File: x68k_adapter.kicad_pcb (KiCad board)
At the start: 2 copper layers, 29 parts, among them J1 USB_A, J2 USB_A, J3 SWD, J4 UART, J5 X68k conn, SW1 SW_Push, U1 PGA2040, U2 USB2422, U3 TPD2EUSB30, U4 TPD2EUSB30, Y1 24MHz

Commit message: recover autosave
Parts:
- C1, C11, C5: footprint Capacitor_THT:C_Disc_D7.5mm_W2.5mm_P5.00mm -> Capacitor_THT:C_Disc_D4.3mm_W1.9mm_P5.00mm
- C10, C12: footprint Capacitor_THT:CP_Radial_D8.0mm_P5.00mm -> Capacitor_THT:CP_Radial_D4.0mm_P2.00mm
- R2, R3, R4: footprint Resistor_THT:R_Axial_DIN0204_L3.6mm_D1.6mm_P7.62mm_Horizontal -> Resistor_SMD:R_0603_1608Metric_Pad0.98x0.95mm_HandSolder; moved to B.Cu
- moved C12 155.5 mm to (191.1, 48.3)
- moved C10 146.6 mm to (198.7, 111.8)
- moved C6 64.5 mm to (103.7, 85.3), turned to 180 degrees
- moved C1 51.7 mm to (111.0, 60.2), turned to 180 degrees
- moved R4 43.0 mm to (94.3, 65.4), turned to 180 degrees
- moved R3 42.4 mm to (94.3, 63.4), turned to 180 degrees
- moved F2 35.9 mm to (183.9, 111.8)
- moved R2 34.9 mm to (99.0, 66.9), turned to 180 degrees
- moved C9 31.4 mm to (186.4, 104.1)
- moved C8 28.9 mm to (87.9, 106.7)
- moved F1 27.4 mm to (181.4, 43.2)
- moved Y1 26.0 mm to (110.0, 79.2), turned to 180 degrees
- moved U4 25.4 mm to (172.4, 106.3)
- moved U3 25.0 mm to (168.1, 40.6), turned to 90 degrees
- moved C5 18.6 mm to (121.2, 73.8), turned to 180 degrees
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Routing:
- net Net-(U2-XTALOUT/CLKIN_EN): track 0.00 -> 18.7 mm
- net Net-(U2-XTALIN/CLKIN): track 0.00 -> 18.6 mm
- net Net-(U2-PLLFILT): track 0.00 -> 12.8 mm
- net Net-(U2-SMBDATA/NON_REM1): track 0.00 -> 11.0 mm, vias 0 -> 1
- net Net-(U2-SMBCLK/CFG_SEL0): track 0.00 -> 10.4 mm, vias 0 -> 1
- net Net-(U2-RBIAS): track 0.00 -> 9.37 mm
- net Net-(U2-SUSP/NON_REM0): track 0.00 -> 5.67 mm, vias 0 -> 1

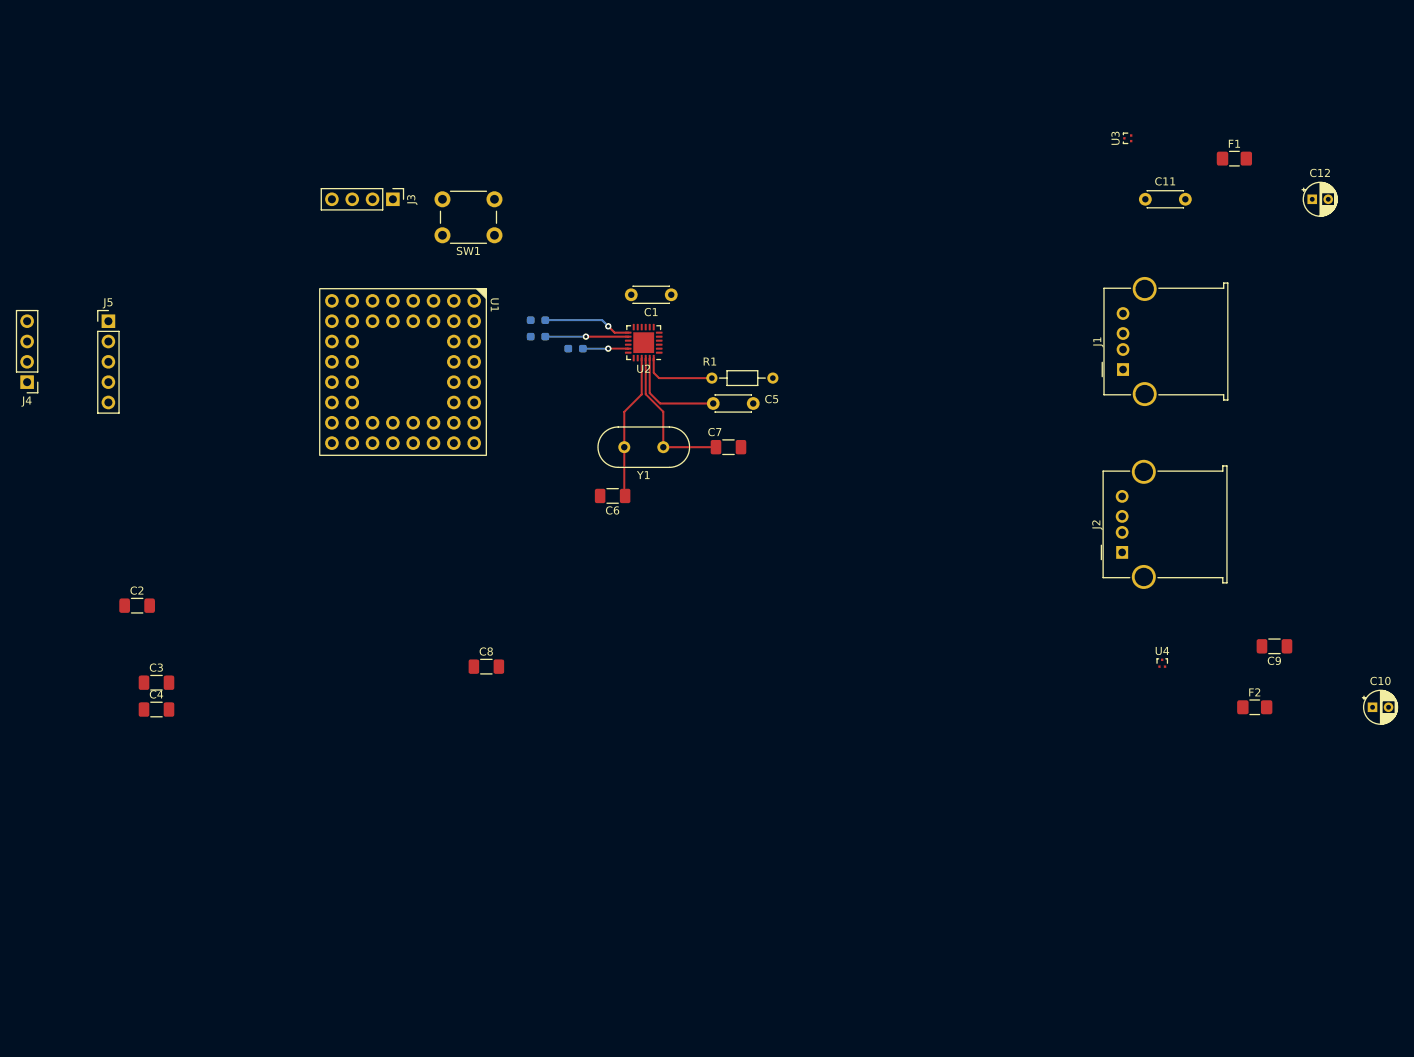
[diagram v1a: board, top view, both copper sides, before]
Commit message: General placement of the components
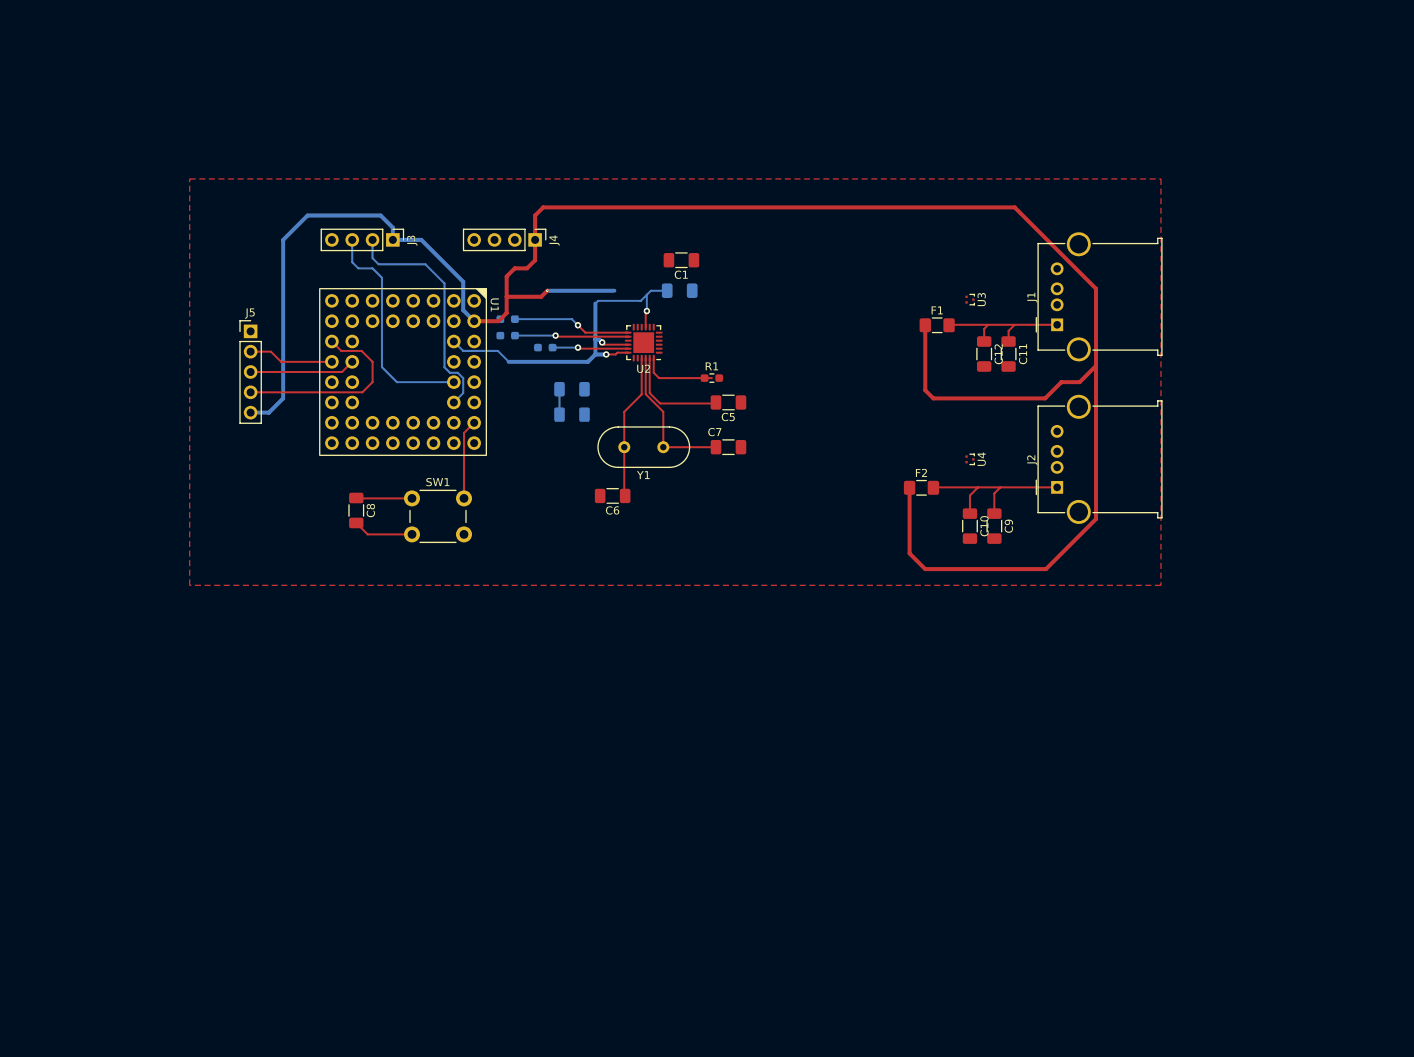
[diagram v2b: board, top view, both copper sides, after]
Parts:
- C1, C11, C5: footprint Capacitor_THT:C_Disc_D4.3mm_W1.9mm_P5.00mm -> Capacitor_SMD:C_1206_3216Metric_Pad1.33x1.80mm_HandSolder
- C10, C12: footprint Capacitor_THT:CP_Radial_D4.0mm_P2.00mm -> Capacitor_SMD:C_1206_3216Metric_Pad1.33x1.80mm_HandSolder
- C2, C3, C4: moved to B.Cu
- R1: footprint Resistor_THT:R_Axial_DIN0204_L3.6mm_D1.6mm_P7.62mm_Horizontal -> Resistor_SMD:R_0603_1608Metric_Pad0.98x0.95mm_HandSolder
- moved C4 83.8 mm to (112.1, 59.7)
- moved J4 65.9 mm to (94.0, 53.3), turned to -90 degrees
- moved C3 61.8 mm to (98.6, 75.2)
- moved C2 60.7 mm to (98.6, 72.0)
- moved C10 55.2 mm to (148.3, 89.1), turned to -90 degrees
- moved F2 49.9 mm to (142.3, 84.3)
- moved C12 45.3 mm to (150.1, 67.6), turned to -90 degrees
- moved F1 42.6 mm to (144.2, 64.0)
- moved C9 38.1 mm to (151.4, 89.1), turned to -90 degrees
- moved U4 35.0 mm to (148.3, 80.8), turned to -90 degrees
- moved SW1 34.5 mm to (78.6, 85.7), turned to 0 degrees
- moved U3 28.2 mm to (148.3, 60.8), turned to -90 degrees
- moved C11 25.8 mm to (153.2, 67.6), turned to -90 degrees
- moved C8 25.4 mm to (71.6, 87.2), turned to -90 degrees
- moved J5 17.8 mm to (58.4, 64.8)
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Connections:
- J4 pad 2: /Tx -> /U_Tx
- J4 pad 3: /Rx -> /U_Rx
- U1 pad B1: /Tx -> /U_Tx
- U1 pad C1: /Rx -> /U_Rx
- U2 pad 2: Net-(J1-D-) -> Net-(J2-D-)
- U2 pad 3: Net-(J1-D+) -> Net-(J2-D+)
- U2 pad 4: Net-(J2-D-) -> Net-(J1-D-)
- U2 pad 5: Net-(J2-D+) -> Net-(J1-D+)
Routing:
- net +5V: track 0.00 -> 261.0 mm, vias 0 -> 1
- net +3V3: track 0.00 -> 51.0 mm, vias 0 -> 3
- net Net-(J3-Pin_2): track 0.00 -> 29.5 mm
- net Net-(J3-Pin_3): track 0.00 -> 28.2 mm
- net /Tx: track 0.00 -> 24.4 mm
- net Net-(J2-VBUS): track 0.00 -> 22.8 mm
- net Net-(J1-VBUS): track 0.00 -> 18.2 mm
- net Net-(U1-BOOTSEL): track 0.00 -> 17.0 mm
- net /Rx: track 0.00 -> 13.2 mm
- net /Mouse: track 0.00 -> 10.7 mm
- net GND: track 0.00 -> 7.55 mm
- net Net-(U2-SUSP/NON_REM0): track 5.67 -> 9.51 mm
- net Net-(U2-SMBCLK/CFG_SEL0): track 10.4 -> 14.2 mm
- net Net-(U2-SMBDATA/NON_REM1): track 11.0 -> 14.9 mm
- added copper zone on F.Cu, net GND

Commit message: Add LCD and finish USB DPs
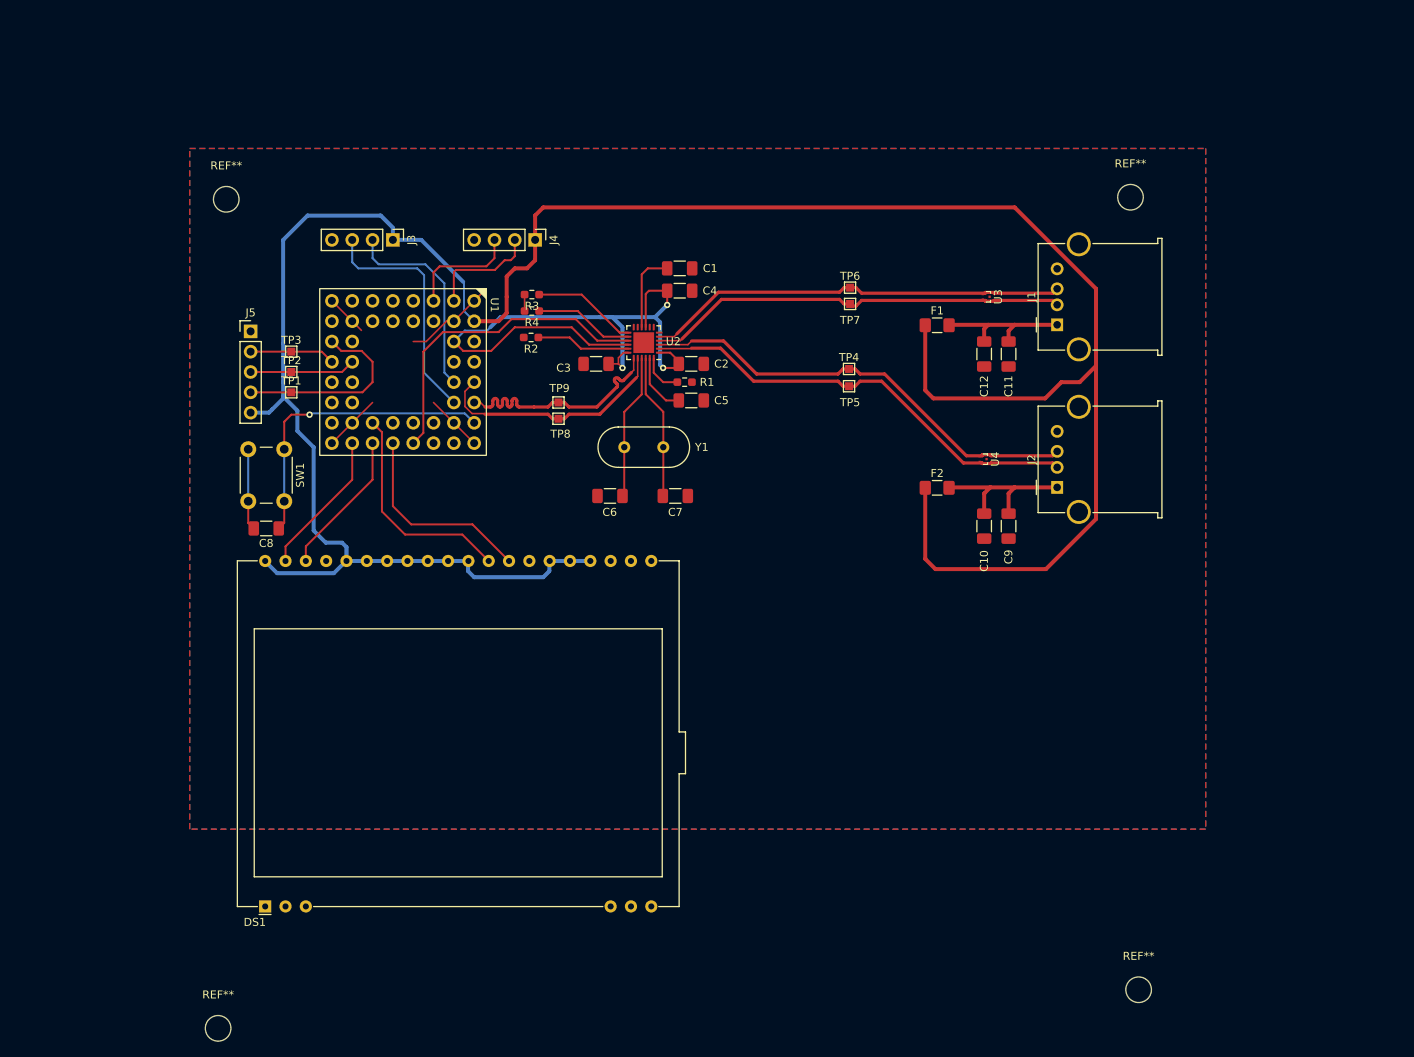
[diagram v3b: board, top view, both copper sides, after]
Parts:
- added DS1: EA_DOGM162S-A, Display:EA_DOGM128-6, F.Cu at (60.2, 136.7)
- added REF**: MountingHole_3.2mm_M3, MountingHole:MountingHole_3.2mm_M3, F.Cu at (169.4, 147.1)
- added REF**: MountingHole_3.2mm_M3, MountingHole:MountingHole_3.2mm_M3, F.Cu at (55.4, 48.3)
- added REF**: MountingHole_3.2mm_M3, MountingHole:MountingHole_3.2mm_M3, F.Cu at (168.4, 48.0)
- added REF**: MountingHole_3.2mm_M3, MountingHole:MountingHole_3.2mm_M3, F.Cu at (54.4, 151.9)
- added TP1: TestPoint, TestPoint:TestPoint_Pad_1.0x1.0mm, F.Cu at (63.5, 72.4)
- added TP2: TestPoint, TestPoint:TestPoint_Pad_1.0x1.0mm, F.Cu at (63.5, 69.8)
- added TP3: TestPoint, TestPoint:TestPoint_Pad_1.0x1.0mm, F.Cu at (63.5, 67.3)
- added TP4: TestPoint, TestPoint:TestPoint_Pad_1.0x1.0mm, F.Cu at (133.2, 69.5)
- added TP5: TestPoint, TestPoint:TestPoint_Pad_1.0x1.0mm, F.Cu at (133.2, 71.6)
- added TP6: TestPoint, TestPoint:TestPoint_Pad_1.0x1.0mm, F.Cu at (133.3, 59.3)
- added TP7: TestPoint, TestPoint:TestPoint_Pad_1.0x1.0mm, F.Cu at (133.3, 61.3)
- added TP8: TestPoint, TestPoint:TestPoint_Pad_1.0x1.0mm, F.Cu at (96.9, 75.7)
- added TP9: TestPoint, TestPoint:TestPoint_Pad_1.0x1.0mm, F.Cu at (96.9, 73.7)
- C2, C3, C4, R2, R3, R4: moved to F.Cu
- moved SW1 17.1 mm to (62.6, 79.5), turned to -90 degrees
- moved C2 15.2 mm to (113.5, 68.8)
- moved C8 11.5 mm to (60.4, 89.4), turned to 180 degrees
- moved C7 9.02 mm to (111.5, 85.3)
- moved C3 7.03 mm to (101.6, 68.8), turned to 180 degrees
- moved C5 4.66 mm to (113.5, 73.4)
- moved R3 4.31 mm to (93.6, 60.2)
- moved R4 4.31 mm to (93.6, 62.2)
- moved R1 3.45 mm to (112.7, 71.1)
- moved R2 2.18 mm to (93.5, 65.5)
- moved U3 2.06 mm to (150.4, 60.5)
- moved F2 1.96 mm to (144.2, 84.3)
- moved C9 1.78 mm to (153.2, 89.1)
- moved C10 1.78 mm to (150.1, 89.1)
- moved U4 1.65 mm to (150.0, 80.7)
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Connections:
- net Net-(J1-D+) renamed /USB_2_D_P
- net Net-(J1-D-) renamed /USB_2_D_N
- net Net-(J2-D+) renamed /USB_1_D_P
- net Net-(J2-D-) renamed /USB_1_D_N
- net Net-(U1-USB_DM) renamed /USB_UP_D_N
- net Net-(U1-USB_DP) renamed /USB_UP_D_P
- U1 pad B5: Net-(J3-Pin_3) -> Net-(J3-Pin_2)
- U1 pad B6: Net-(J3-Pin_2) -> Net-(J3-Pin_3)
- U1 pad E8: unconnected-(U1-GPIO23-PadE8) -> /SPI Tx
- U1 pad F7: unconnected-(U1-GPIO22-PadF7) -> /SPI SCK
- U1 pad F8: unconnected-(U1-GPIO21-PadF8) -> /SPI CSn
- U1 pad G8: unconnected-(U1-GPIO20-PadG8) -> Net-(DS1-RS)
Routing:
- net /USB_1_D_P: track 0.00 -> 56.9 mm
- net /USB_1_D_N: track 0.00 -> 56.6 mm
- net +5V: track 261.0 -> 315.8 mm, vias 1 -> 0
- net /USB_2_D_P: track 0.00 -> 53.0 mm
- net /USB_2_D_N: track 0.00 -> 52.8 mm
- net GND: track 7.55 -> 48.7 mm
- net /HUBRST: track 0.00 -> 40.4 mm
- net +3V3: track 51.0 -> 86.6 mm
- net /USB_UP_D_P: track 0.00 -> 30.2 mm
- net /USB_UP_D_N: track 0.00 -> 30.0 mm
- net /SPI SCK: track 0.00 -> 27.5 mm
- net /SPI Tx: track 0.00 -> 25.2 mm
- net Net-(U1-BOOTSEL): track 17.0 -> 38.3 mm, vias 0 -> 1
- net Net-(DS1-RS): track 0.00 -> 18.2 mm
- net /SPI CSn: track 0.00 -> 18.2 mm
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- added copper zone on B.Cu, net GND
- added copper zone on In1.Cu, net GND
- added copper zone on In2.Cu, net GND
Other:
- copper layers 2 -> 4

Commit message: Fix LCD footprint
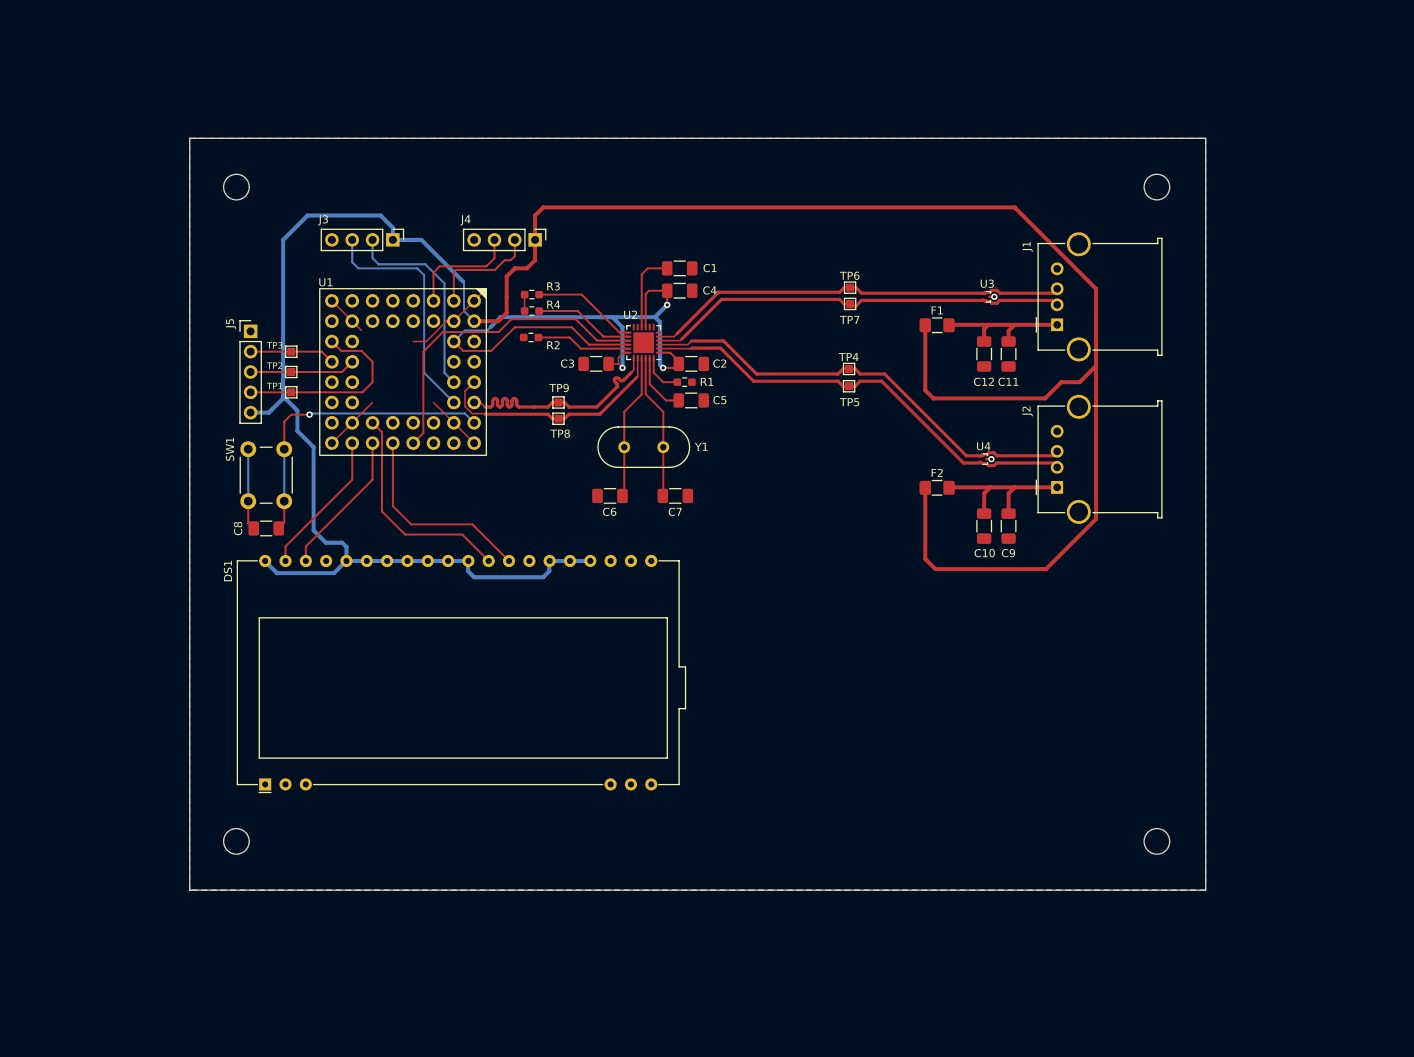
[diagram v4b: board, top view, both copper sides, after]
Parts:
- moved REF** 23.5 mm to (56.6, 128.5)
- moved REF** 18.7 mm to (171.7, 128.5)
- moved REF** 3.54 mm to (171.7, 46.7)
- moved REF** 1.98 mm to (56.6, 46.7)
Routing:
- net GND: track 48.7 -> 49.9 mm, vias 0 -> 2
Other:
- board outline added: 127 x 94 mm

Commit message: Final placement
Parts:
- moved REF** 25.1 mm to (50.8, 104.1)
- moved REF** 24.5 mm to (168.9, 104.1)
- moved J4 21.6 mm to (94.0, 31.8)
- moved J3 21.6 mm to (76.2, 31.8)
- moved SW1 17.3 mm to (55.0, 64.0)
- moved C8 17.1 mm to (53.0, 74.0)
- moved J5 17.0 mm to (50.8, 49.5)
- moved TP1 16.5 mm to (57.1, 57.1)
- moved TP3 16.5 mm to (57.1, 52.1)
- moved TP2 16.5 mm to (57.1, 54.6)
- moved REF** 16.3 mm to (50.8, 31.5)
- moved REF** 15.5 mm to (168.9, 31.5)
- moved C11 15.2 mm to (153.2, 52.4)
- moved C12 15.2 mm to (150.1, 52.4)
- moved C5 15.2 mm to (113.5, 58.2)
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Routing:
- net +5V: track 315.8 -> 352.0 mm
- net /Mouse: track 10.7 -> 18.3 mm
- net /Tx: track 24.4 -> 32.1 mm
- net /Rx: track 13.2 -> 20.8 mm
- net Net-(U1-BOOTSEL): track 38.3 -> 45.0 mm
- net /U_Rx: track 14.2 -> 20.6 mm
- net Net-(J3-Pin_3): track 29.9 -> 36.2 mm
- net Net-(J3-Pin_2): track 25.4 -> 31.8 mm
- net /U_Tx: track 14.1 -> 20.0 mm
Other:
- board size 127 x 94 mm -> 130.8 x 85.1 mm
- board text added: "X2468 v0.1- USB adapter for Sharp X68000"
- board text added: "https://github.com/spookbench/X2468"
- board text added: "spook & polprog 2023 <3"
